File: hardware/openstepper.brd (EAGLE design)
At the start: 100 x 80 mm, 9 parts, among them IC1 DARLINGTON_ARRAY, J1 CON_HEADER_1X06-PTH, J2 CON_HEADER_1X05-PTH, J3 CON_HEADER_1X04

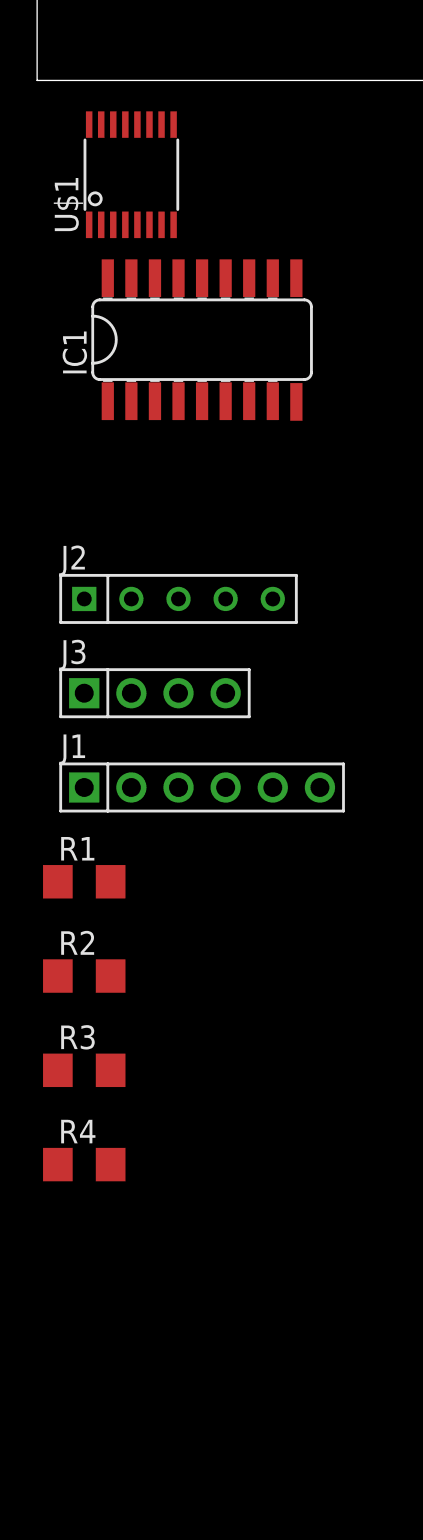
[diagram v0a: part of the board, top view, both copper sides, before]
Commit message: change symbol in lib, schema updated
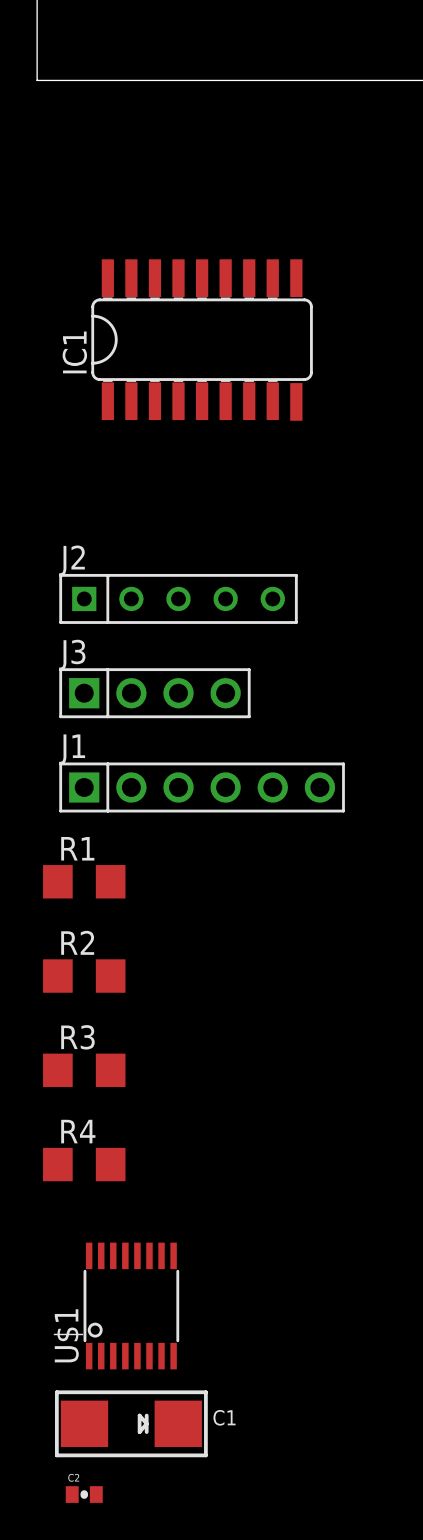
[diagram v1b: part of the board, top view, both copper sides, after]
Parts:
- added C1: 4.7uF, microbuilder:EIA6032-28/C-R
- added C2: 10nF, SparkFun-Capacitors:0402-CAP
- moved U$1 61.0 mm to (5.08, -66.0)
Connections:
- removed net N$11: J1.4, R4.1, U$1.7
- removed net N$12: J1.2, U$1.16
- new net N$14: J1.4, R2.1, U$1.7
- net GND: now also C1.-, C2.2
- net INIT: now also R1.1; no longer R3.1
- net N$5: now also R4.1; no longer R1.1
- net N$7: now also R3.1
- net VDD: now also C1.+, C2.1, U$1.16
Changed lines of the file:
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@@
 </autorouter>
 <elements>
-<element name="U$1" library="openstepper" package="TSSOP-16" value="IC_PCA9629A" x="5.08" y="-5.08"/>
 <element name="IC1" library="openstepper" package="SO-18" value="DARLINGTON_ARRAY" x="8.89" y="-13.97"/>
 <element name="J2" library="dp_devices" package="M1X5" value="CON_HEADER_1X05-PTH" x="7.62" y="-27.94"/>
@@
 <element name="R3" library="dp_devices" package="R1206" value="1k6" x="2.54" y="-53.34"/>
 <element name="R4" library="dp_devices" package="R1206" value="1k6" x="2.54" y="-58.42"/>
+<element name="U$1" library="openstepper" package="TSSOP-16" value="IC_PCA9629A" x="5.08" y="-66.04"/>
+<element name="C1" library="microbuilder" package="EIA6032-28/C-R" value="4.7uF" x="5.08" y="-72.39"/>
+<element name="C2" library="SparkFun-Capacitors" package="0402-CAP" value="10nF" x="2.54" y="-76.2">
+<attribute name="PROD_ID" value="CAP-00867" x="2.54" y="-76.2" size="1.778" layer="27" display="off"/>
+</element>
 </elements>
 <signals>
 <signal name="N$1">
-<contactref element="U$1" pad="12"/>
 <contactref element="IC1" pad="1"/>
 <contactref element="IC1" pad="2"/>
 <contactref element="J2" pad="1"/>
+<contactref element="U$1" pad="12"/>
+<wire x1="2.54" y1="-27.94" x2="5.405" y2="-63.34" width="0" layer="19" extent="1-1"/>
 <wire x1="3.81" y1="-17.2847" x2="2.54" y2="-27.94" width="0" layer="19" extent="1-1"/>
 <wire x1="5.08" y1="-17.2847" x2="3.81" y2="-17.2847" width="0" layer="19" extent="1-1"/>
-<wire x1="5.405" y1="-2.38" x2="5.08" y2="-17.2847" width="0" layer="19" extent="1-1"/>
 </signal>
 <signal name="N$2">
-<contactref element="U$1" pad="11"/>
 <contactref element="IC1" pad="3"/>
 <contactref element="IC1" pad="4"/>
 <contactref element="J2" pad="2"/>
+<contactref element="U$1" pad="11"/>
+<wire x1="5.08" y1="-27.94" x2="6.055" y2="-63.34" width="0" layer="19" extent="1-1"/>
 <wire x1="6.35" y1="-17.2847" x2="5.08" y2="-27.94" width="0" layer="19" extent="1-1"/>
 <wire x1="7.62" y1="-17.2847" x2="6.35" y2="-17.2847" width="0" layer="19" extent="1-1"/>
-<wire x1="6.055" y1="-2.38" x2="6.35" y2="-17.2847" width="0" layer="19" extent="1-1"/>
 </signal>
 <signal name="N$3">
-<contactref element="U$1" pad="10"/>
 <contactref element="IC1" pad="5"/>
 <contactref element="IC1" pad="6"/>
 <contactref element="J2" pad="3"/>
+<contactref element="U$1" pad="10"/>
+<wire x1="7.62" y1="-27.94" x2="6.705" y2="-63.34" width="0" layer="19" extent="1-1"/>
 <wire x1="8.89" y1="-17.2847" x2="7.62" y2="-27.94" width="0" layer="19" extent="1-1"/>
 <wire x1="10.16" y1="-17.2847" x2="8.89" y2="-17.2847" width="0" layer="19" extent="1-1"/>
-<wire x1="6.705" y1="-2.38" x2="8.89" y2="-17.2847" width="0" layer="19" extent="1-1"/>
 </signal>
 <signal name="N$4">
-<contactref element="U$1" pad="9"/>
 <contactref element="IC1" pad="7"/>
 <contactref element="IC1" pad="8"/>
 <contactref element="J2" pad="4"/>
+<contactref element="U$1" pad="9"/>
+<wire x1="10.16" y1="-27.94" x2="7.355" y2="-63.34" width="0" layer="19" extent="1-1"/>
 <wire x1="11.43" y1="-17.2847" x2="10.16" y2="-27.94" width="0" layer="19" extent="1-1"/>
 <wire x1="12.7" y1="-17.2847" x2="11.43" y2="-17.2847" width="0" layer="19" extent="1-1"/>
-<wire x1="7.355" y1="-2.38" x2="11.43" y2="-17.2847" width="0" layer="19" extent="1-1"/>
 </signal>
 <signal name="GND">
 <contactref element="IC1" pad="9"/>
-<contactref element="U$1" pad="8"/>
 <contactref element="J2" pad="5"/>
 <contactref element="J1" pad="1"/>
+<contactref element="U$1" pad="8"/>
+<contactref element="C1" pad="-"/>
+<contactref element="C2" pad="2"/>
+<wire x1="2.555" y1="-72.39" x2="3.19" y2="-76.2" width="0" layer="19" extent="1-1"/>
+<wire x1="7.355" y1="-68.74" x2="2.555" y2="-72.39" width="0" layer="19" extent="1-1"/>
+<wire x1="2.54" y1="-38.1" x2="7.355" y2="-68.74" width="0" layer="19" extent="1-1"/>
 <wire x1="12.7" y1="-27.94" x2="2.54" y2="-38.1" width="0" layer="19" extent="1-1"/>
 <wire x1="13.97" y1="-17.3229" x2="12.7" y2="-27.94" width="0" layer="19" extent="1-1"/>
-<wire x1="7.355" y1="-7.78" x2="13.97" y2="-17.3229" width="0" layer="19" extent="1-1"/>
 </signal>
 <signal name="N$6">
@@
 </signal>
 <signal name="N$5">
+<contactref element="J1" pad="6"/>
 <contactref element="U$1" pad="14"/>
-<contactref element="J1" pad="6"/>
-<contactref element="R1" pad="1"/>
-<wire x1="15.24" y1="-38.1" x2="1.118" y2="-43.18" width="0" layer="19" extent="1-1"/>
-<wire x1="4.105" y1="-2.38" x2="15.24" y2="-38.1" width="0" layer="19" extent="1-1"/>
+<contactref element="R4" pad="1"/>
+<wire x1="1.118" y1="-58.42" x2="4.105" y2="-63.34" width="0" layer="19" extent="1-1"/>
+<wire x1="15.24" y1="-38.1" x2="1.118" y2="-58.42" width="0" layer="19" extent="1-1"/>
 </signal>
 <signal name="N$7">
 <contactref element="J1" pad="5"/>
 <contactref element="U$1" pad="15"/>
-<wire x1="3.455" y1="-2.38" x2="12.7" y2="-38.1" width="0" layer="19" extent="1-1"/>
-</signal>
-<signal name="N$11">
-<contactref element="U$1" pad="7"/>
-<contactref element="J1" pad="4"/>
-<contactref element="R4" pad="1"/>
-<wire x1="10.16" y1="-38.1" x2="1.118" y2="-58.42" width="0" layer="19" extent="1-1"/>
-<wire x1="6.705" y1="-7.78" x2="10.16" y2="-38.1" width="0" layer="19" extent="1-1"/>
+<contactref element="R3" pad="1"/>
+<wire x1="1.118" y1="-53.34" x2="3.455" y2="-63.34" width="0" layer="19" extent="1-1"/>
+<wire x1="12.7" y1="-38.1" x2="1.118" y2="-53.34" width="0" layer="19" extent="1-1"/>
 </signal>
 <signal name="INIT">
+<contactref element="J1" pad="3"/>
 <contactref element="U$1" pad="13"/>
-<contactref element="J1" pad="3"/>
-<contactref element="R3" pad="1"/>
-<wire x1="7.62" y1="-38.1" x2="1.118" y2="-53.34" width="0" layer="19" extent="1-1"/>
-<wire x1="4.755" y1="-2.38" x2="7.62" y2="-38.1" width="0" layer="19" extent="1-1"/>
-</signal>
-<signal name="N$12">
-<contactref element="J1" pad="2"/>
-<contactref element="U$1" pad="16"/>
-<wire x1="2.805" y1="-2.38" x2="5.08" y2="-38.1" width="0" layer="19" extent="1-1"/>
+<contactref element="R1" pad="1"/>
+<wire x1="1.118" y1="-43.18" x2="4.755" y2="-63.34" width="0" layer="19" extent="1-1"/>
+<wire x1="7.62" y1="-38.1" x2="1.118" y2="-43.18" width="0" layer="19" extent="1-1"/>
 </signal>
 <signal name="VDD">
@@
 <contactref element="R3" pad="2"/>
 <contactref element="R2" pad="2"/>
+<contactref element="U$1" pad="16"/>
+<contactref element="C2" pad="1"/>
+<contactref element="C1" pad="+"/>
+<wire x1="7.605" y1="-72.39" x2="1.89" y2="-76.2" width="0" layer="19" extent="1-1"/>
+<wire x1="2.805" y1="-63.34" x2="7.605" y2="-72.39" width="0" layer="19" extent="1-1"/>
+<wire x1="3.962" y1="-58.42" x2="2.805" y2="-63.34" width="0" layer="19" extent="1-1"/>
 <wire x1="3.962" y1="-53.34" x2="3.962" y2="-58.42" width="0" layer="19" extent="1-1"/>
 <wire x1="3.962" y1="-48.26" x2="3.962" y2="-53.34" width="0" layer="19" extent="1-1"/>
 <wire x1="3.962" y1="-43.18" x2="3.962" y2="-48.26" width="0" layer="19" extent="1-1"/>
 </signal>
+<signal name="N$14">
+<contactref element="J1" pad="4"/>
+<contactref element="U$1" pad="7"/>
+<contactref element="R2" pad="1"/>
+<wire x1="1.118" y1="-48.26" x2="6.705" y2="-68.74" width="0" layer="19" extent="1-1"/>
+<wire x1="10.16" y1="-38.1" x2="1.118" y2="-48.26" width="0" layer="19" extent="1-1"/>
+</signal>
 </signals>

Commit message: schema update + datasheets
missing power regulator and optocopler setup (change to PC817)
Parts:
- removed J2: CON_HEADER_1X05-PTH, dp_devices:M1X5
- added J4: CON_HEADER_1X02-PTH, dp_devices:M1X2
- added JP1, JP2: (no value), microbuilder:2X08
- added LED1, LED2: (no value), dp_devices:LED-805
- added R5, R6: (no value), dp_devices:R805
- added U$7, U$8: TCMT1103-OPTO, SparkFun-DiscreteSemi:SSOP-4
- C1: device microbuilder:EIA6032-28/C-R -> microbuilder:PANASONIC_C
- C2: value 10nF -> 0.01uF; device SparkFun-Capacitors:0402-CAP -> dp_devices:C805
- moved C2 11.4 mm to (2.54, -87.6)
- renumbered U$1 to U1
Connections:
- new net AD0: JP2.5
- new net AD1: JP2.6
- new net CSL: JP2.14
- new net INT: JP2.13
- new net N$11: LED1.A, R5.1
- new net N$12: LED2.C, U1.4
- new net N$13: LED1.C, U1.3
- new net N$15: LED2.A, R6.1
- new net N$16: JP1.1, JP1.3, JP1.5, JP1.7, U1.5
- new net N$17: JP1.11, JP1.13, JP1.15, JP1.9, U1.6
- new net OUT0: JP2.12
- new net OUT1: JP2.11
- new net OUT2: JP2.10
- new net OUT3: JP2.9
- new net P0/DET: JP2.1
- new net P1: JP2.2
- new net P2: JP2.3
- new net P3: JP2.4
- new net RESET: JP2.7
- new net SDA: JP2.15
- new net VSS: JP2.8
- net +12V: now also J4.1
- net GND: now also J4.2, JP1.10, JP1.2; no longer J2.5
- net N$1: no longer J2.1
- net N$2: no longer J2.2
- net N$3: no longer J2.3
- net N$4: no longer J2.4
- net N$5: now also JP1.4, JP1.6
- net VDD: now also JP1.16, JP1.8, JP2.16, R5.2, R6.2

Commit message: rough board layout
and split breakout into two parts, also fixed names and labels on
breakout
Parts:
- removed JP2: (no value), microbuilder:2X08
- added JP3, JP4: (no value), adafruit:1X08-BIG
- moved U$8 157.0 mm to (49.8, 30.5), turned to 270 degrees
- moved U$7 151.7 mm to (45.8, 30.2), turned to 270 degrees
- moved LED2 117.9 mm to (18.0, 16.6), turned to 270 degrees
- moved R5 116.8 mm to (13.3, 20.4), turned to 180 degrees
- moved R6 116.8 mm to (13.2, 16.6), turned to 180 degrees
- moved JP1 110.9 mm to (13.3, 4.95)
- moved LED1 110.3 mm to (18.4, 20.4), turned to 270 degrees
- moved C2 101.8 mm to (30.9, 10.2)
- moved J4 99.2 mm to (48.4, 7.37), turned to 270 degrees
- moved U1 87.4 mm to (27.6, 18.4), turned to 270 degrees
- moved C1 80.8 mm to (30.7, 4.19), turned to 180 degrees
- moved R4 80.2 mm to (7.75, 21.6)
- moved R3 79.3 mm to (13.0, 25.3)
- moved R2 76.3 mm to (7.87, 27.8)
- moved R1 74.2 mm to (13.1, 30.2)
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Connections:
- removed net CSL: JP2.14
- removed net INIT: J1.3, R1.1, U1.13
- removed net N$1: IC1.1, IC1.2, U1.12
- removed net N$12: LED2.C, U1.4
- removed net N$13: LED1.C, U1.3
- removed net N$14: J1.4, R2.1, U1.7
- removed net N$16: JP1.1, JP1.3, JP1.5, JP1.7, U1.5
- removed net N$17: JP1.11, JP1.13, JP1.15, JP1.9, U1.6
- removed net N$2: IC1.3, IC1.4, U1.11
- removed net N$3: IC1.5, IC1.6, U1.10
- removed net N$4: IC1.7, IC1.8, U1.9
- removed net N$5: J1.6, JP1.4, JP1.6, R4.1, U1.14
- removed net N$7: J1.5, R3.1, U1.15
- new net SCL: J1.6, JP1.4, JP1.6, JP3.3, R4.1, U1.14
- net AD0: now also JP1.1, JP1.3, JP1.5, JP1.7, JP4.4, U1.5; no longer JP2.5
- net AD1: now also JP1.11, JP1.13, JP1.15, JP1.9, JP4.3, U1.6; no longer JP2.6
- net INT: now also J1.3, JP3.4, R1.1, U1.13; no longer JP2.13
- net OUT0: now also IC1.1, IC1.2, JP3.5, U1.12; no longer JP2.12
- net OUT1: now also IC1.3, IC1.4, JP3.6, U1.11; no longer JP2.11
- net OUT2: now also IC1.5, IC1.6, JP3.7, U1.10; no longer JP2.10
- net OUT3: now also IC1.7, IC1.8, JP3.8, U1.9; no longer JP2.9
- net P0/DET: now also JP4.8, U1.1; no longer JP2.1
- net P1: now also JP4.7, U1.2; no longer JP2.2
- net P2: now also JP4.6, LED1.C, U1.3; no longer JP2.3
- net P3: now also JP4.5, LED2.C, U1.4; no longer JP2.4
- net RESET: now also J1.4, JP4.2, R2.1, U1.7; no longer JP2.7
- net SDA: now also J1.5, JP3.2, R3.1, U1.15; no longer JP2.15
- net VDD: now also JP3.1; no longer JP2.16
- net VSS: now also JP4.1; no longer JP2.8
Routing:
- added copper zone on layer 1, net GND
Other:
- board size 100 x 80 mm -> 54.6 x 38.1 mm
- board text added: "openStepper"

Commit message: added 5v regulator to schema
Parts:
- added C3: 330nF, rcl:C025-024X044
- added C4: 100nF, rcl:C025-024X044
- added IC2: 7805DT, adafruit:TO252
- added LED3: (no value), dp_devices:LED-805
- added R8: 1k5, dp_devices:R1206
- moved U$8 21.2 mm to (28.6, 29.7)
- moved U$7 20.6 mm to (25.3, 29.6)
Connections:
- new net N$1: LED3.A, R8.1
- new net V_MOT: C3.2, IC2.1
- net GND: now also C3.1, C4.1, IC2.3, LED3.C
- net VDD: now also C4.2, IC2.2, R8.2
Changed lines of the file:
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@@
 <element name="LED2" library="dp_devices" package="LED-805" value="" x="18.034" y="16.637" rot="R270"/>
 <element name="JP1" library="microbuilder" package="2X08" value="" x="13.335" y="4.953"/>
-<element name="U$7" library="SparkFun-DiscreteSemi" package="SSOP-4" value="TCMT1103-OPTO" x="45.847" y="30.226" rot="R270"/>
-<element name="U$8" library="SparkFun-DiscreteSemi" package="SSOP-4" value="TCMT1103-OPTO" x="49.784" y="30.48" rot="R270"/>
+<element name="U$7" library="SparkFun-DiscreteSemi" package="SSOP-4" value="TCMT1103-OPTO" x="25.273" y="29.591" rot="R270"/>
+<element name="U$8" library="SparkFun-DiscreteSemi" package="SSOP-4" value="TCMT1103-OPTO" x="28.575" y="29.718" rot="R270"/>
 <element name="JP3" library="adafruit" package="1X08-BIG" value="" x="34.163" y="19.304" rot="R270"/>
 <element name="JP4" library="adafruit" package="1X08-BIG" value="" x="21.209" y="19.558" rot="R90"/>
+<element name="C3" library="rcl" package="C025-024X044" value="330nF" x="66.929" y="22.098" rot="R180"/>
+<element name="C4" library="rcl" package="C025-024X044" value="100nF" x="69.469" y="28.448"/>
+<element name="R8" library="dp_devices" package="R1206" value="1k5" x="74.803" y="30.734" rot="R90"/>
+<element name="LED3" library="dp_devices" package="LED-805" value="" x="74.803" y="26.543" rot="R180"/>
+<element name="IC2" library="adafruit" package="TO252" value="7805DT" x="68.453" y="36.957"/>
 </elements>
 <signals>
@@
 <vertex x="-0.254" y="0.127"/>
 </polygon>
+<contactref element="C4" pad="1"/>
+<contactref element="C3" pad="1"/>
+<contactref element="LED3" pad="C"/>
+<contactref element="IC2" pad="3"/>
+<wire x1="68.199" y1="28.448" x2="68.453" y2="39.457" width="0" layer="19" extent="1-1"/>
+<wire x1="68.199" y1="22.098" x2="68.199" y2="28.448" width="0" layer="19" extent="1-1"/>
+<wire x1="74.803" y1="25.493" x2="68.199" y2="28.448" width="0" layer="19" extent="1-1"/>
+<wire x1="48.387" y1="6.096" x2="68.199" y2="22.098" width="0" layer="19" extent="1-1"/>
 </signal>
 <signal name="N$6">
@@
 <contactref element="C2" pad="1"/>
 <contactref element="JP3" pad="1"/>
+<contactref element="C4" pad="2"/>
+<contactref element="R8" pad="2"/>
+<contactref element="IC2" pad="2"/>
+<wire x1="70.733" y1="32.157" x2="74.803" y2="32.156" width="0" layer="19" extent="1-1"/>
+<wire x1="70.739" y1="28.448" x2="70.733" y2="32.157" width="0" layer="19" extent="1-1"/>
+<wire x1="34.163" y1="28.194" x2="70.739" y2="28.448" width="0" layer="19" extent="1-1"/>
 <wire x1="30.259" y1="20.69" x2="34.163" y2="28.194" width="0" layer="19" extent="1-1"/>
 <wire x1="29.911" y1="10.16" x2="30.259" y2="20.69" width="0" layer="19" extent="1-1"/>
@@
 <contactref element="JP4" pad="3"/>
 <wire x1="21.209" y1="15.748" x2="24.859" y2="17.44" width="0" layer="19" extent="1-1"/>
-<wire x1="19.685" y1="3.683" x2="21.209" y2="15.748" width="0" layer="19" extent="1-1"/>
-<wire x1="22.225" y1="3.683" x2="19.685" y2="3.683" width="0" layer="19" extent="1-1"/>
+<wire x1="22.225" y1="3.683" x2="21.209" y2="15.748" width="0" layer="19" extent="1-1"/>
+<wire x1="19.685" y1="3.683" x2="22.225" y2="3.683" width="0" layer="19" extent="1-1"/>
 <wire x1="17.145" y1="3.683" x2="19.685" y2="3.683" width="0" layer="19" extent="1-1"/>
 <wire x1="14.605" y1="3.683" x2="17.145" y2="3.683" width="0" layer="19" extent="1-1"/>
@@
 <contactref element="JP4" pad="1"/>
 </signal>
+<signal name="N$1">
+<contactref element="LED3" pad="A"/>
+<contactref element="R8" pad="1"/>
+<wire x1="74.803" y1="27.593" x2="74.803" y2="29.312" width="0" layer="19" extent="1-1"/>
+</signal>
+<signal name="V_MOT">
+<contactref element="IC2" pad="1"/>
+<contactref element="C3" pad="2"/>
+<wire x1="65.659" y1="22.098" x2="66.173" y2="32.157" width="0" layer="19" extent="1-1"/>
+</signal>
 </signals>
